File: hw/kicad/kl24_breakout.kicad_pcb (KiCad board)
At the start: 2 copper layers, 36.1 x 20.8 mm, 53 parts, among them J1 USB-micro-ab, P1 TST, P10 TST, P11 TST, P12 TST, P13 TST, P14 TST, P15 TST, P16 TST, P17 TST, P18 TST, P19 TST, P2 TST, P20 TST, P21 TST, P22 TST, P23 TST, P24 TST, P25 TST, P26 TST, P27 TST, P28 TST, P29 TST, P3 TST, P30 TST, P31 TST, P32 TST, P33 USB_V, P34 USB_GND, P35 SWD_VCC, P36 SWDIO, P37 SWCLK, P38 NRESET, P39 SWD_GND, P4 TST, P5 TST, P6 TST, P7 TST, P8 TST, P9 TST, U1 MKL24Z64VFM4, U2 LP3985, X1 CRYSTAL

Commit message: more pcb
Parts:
- C1, C2, C3, C4, D1, J1, JP1, R1, R2, R3, R4, U2: moved to B.Cu
- P33: value USB_V -> 5V
- P34: value USB_GND -> GND
- P35: value SWD_VCC -> 3.3V; footprint TEST_0.100 -> smd_simple_pad; moved to B.Cu
- P36, P37: footprint TEST_0.100 -> smd_simple_pad; moved to B.Cu
- P38: value NRESET -> NRST; footprint TEST_0.100 -> smd_simple_pad; moved to B.Cu
- P39: value SWD_GND -> GND; footprint TEST_0.100 -> smd_simple_pad; moved to B.Cu
- moved P38 39.1 mm to (141.7, 69.1), turned to 90 degrees
- moved P37 37.5 mm to (141.7, 67.1), turned to 90 degrees
- moved P36 34.8 mm to (141.7, 71.1), turned to 90 degrees
- moved P39 30.6 mm to (141.7, 73.2), turned to 90 degrees
- moved P35 30.1 mm to (141.7, 75.2), turned to 90 degrees
- moved U2 27.9 mm to (119.1, 67.8), turned to 90 degrees
- moved R3 18.1 mm to (119.6, 73.9)
- moved C4 17.7 mm to (121.4, 70.9)
- moved R4 8.40 mm to (133.6, 84.6)
- moved R1 6.28 mm to (122.9, 87.9)
- moved C2 5.80 mm to (136.1, 87.4)
- moved R2 5.61 mm to (127.5, 88.6)
- moved C3 4.60 mm to (129.3, 84.8)
- moved C1 4.34 mm to (131.8, 88.1)
- moved JP1 2.84 mm to (139.7, 85.3)
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
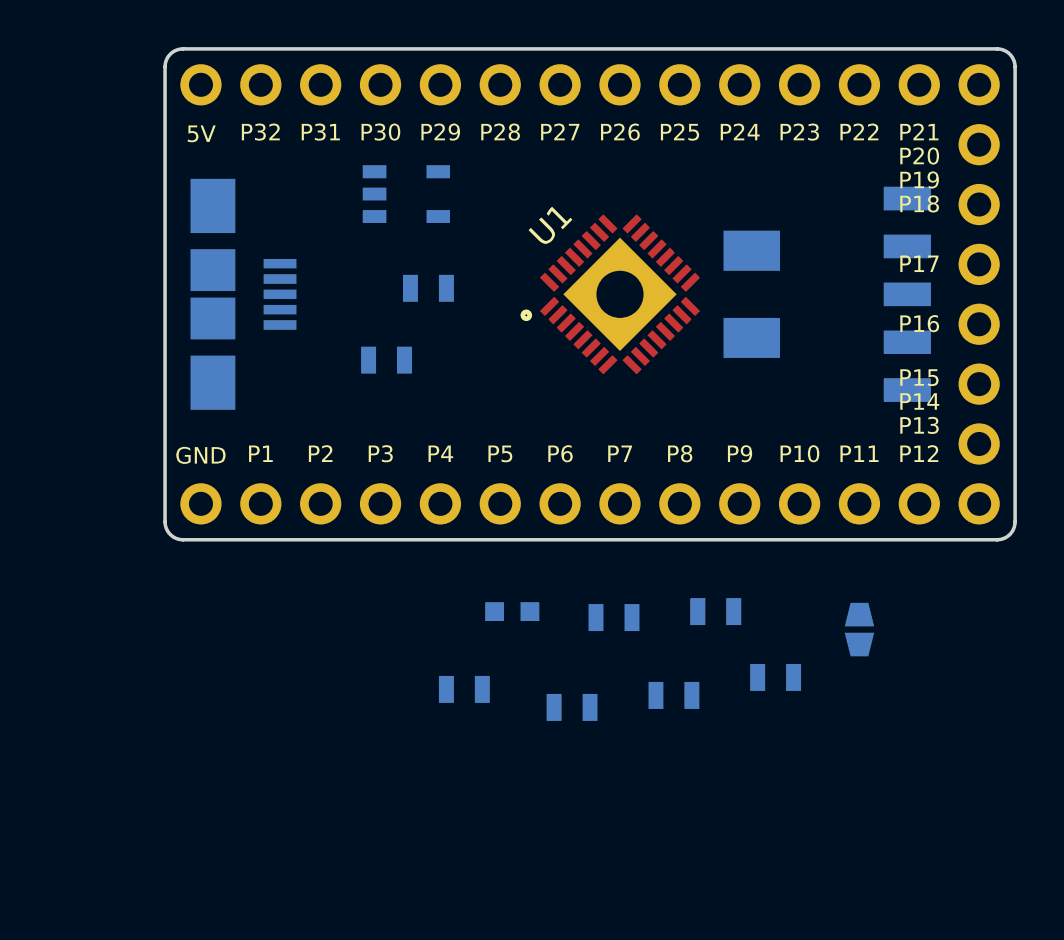
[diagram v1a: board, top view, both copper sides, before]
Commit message: all footprints placed, start wiring
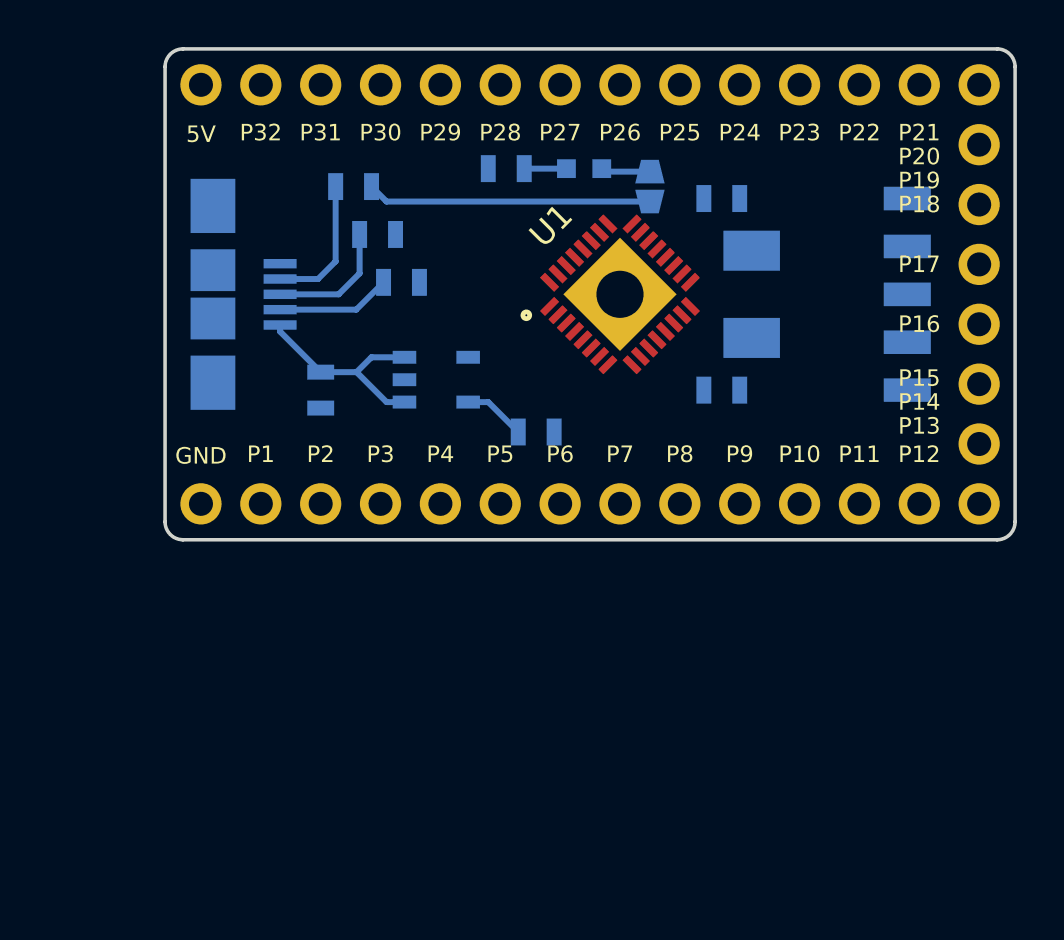
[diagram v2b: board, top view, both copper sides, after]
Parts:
- moved C1 21.2 mm to (133.9, 67.1), turned to 180 degrees
- moved R4 20.8 mm to (124.7, 65.8), turned to 180 degrees
- moved JP1 20.8 mm to (130.8, 66.5)
- moved R1 19.7 mm to (119.3, 68.6)
- moved R2 19.4 mm to (120.3, 70.6)
- moved D1 19.0 mm to (128.0, 65.8), turned to 180 degrees
- moved C3 15.8 mm to (116.8, 75.2), turned to 270 degrees
- moved C2 12.4 mm to (133.9, 75.2), turned to 180 degrees
- moved U2 7.98 mm to (120.4, 75.7)
- moved C4 7.62 mm to (126.0, 77.0)
- moved R3 7.50 mm to (118.2, 66.5)
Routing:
- net 20: track 0.00 -> 12.1 mm
- net USB_VBUS: track 0.00 -> 9.10 mm
- net Net-<J1-Pad4>: track 0.00 -> 5.84 mm
- net USB_DP: track 0.00 -> 5.39 mm
- net USB_DM: track 0.00 -> 4.87 mm
- net 7: track 0.00 -> 2.65 mm
- net Net-<D1-Pad1>: track 0.00 -> 2.10 mm
- net Net-<D1-Pad2>: track 0.00 -> 1.79 mm

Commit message: most connections
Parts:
- P33: value 5V -> USB_V
- P34: value GND -> USB_GND
- P35: value 3.3V -> SWD_VCC
- P38: value NRST -> NRESET
- P39: value GND -> SWD_GND
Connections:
- net Net-<D1-Pad1> renamed N-0000030
- net Net-<D1-Pad2> renamed N-0000031
- net Net-<J1-Pad4> renamed N-0000029
- C1 pad 2: 8 -> 16
- C2 pad 2: 8 -> 16
- C3 pad 2: 8 -> 16
- C4 pad 1: 7 -> 15
- C4 pad 2: 8 -> 16
- J1 pad 5: 8 -> 16
- J1 pad 6: 8 -> 16
- P2 pad 1: 8 -> 16
- P34 pad 1: 8 -> 16
- P35 pad 1: 7 -> 15
- P39 pad 1: 8 -> 16
- P7 pad 1: 7 -> 15
- P8 pad 1: 8 -> 16
- R4 pad 2: 8 -> 16
- U1 pad 2: 8 -> 16
- U1 pad 7: 7 -> 15
- U1 pad 8: 8 -> 16
- U2 pad 2: 8 -> 16
- U2 pad 4: Net-<U2-Pad4> -> (no net)
- U2 pad 5: 7 -> 15
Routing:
- net 16: track 0.00 -> 33.1 mm
- net 15: track 0.00 -> 23.6 mm
- net 20: track 12.1 -> 28.4 mm
- net 13: track 0.00 -> 16.3 mm
- net 18: track 0.00 -> 16.2 mm
- net 32: track 0.00 -> 15.7 mm
- net 1: track 0.00 -> 15.7 mm
- net 14: track 0.00 -> 15.1 mm
- net 19: track 0.00 -> 15.1 mm
- net 17: track 0.00 -> 15.0 mm
- net 21: track 0.00 -> 14.3 mm
- net 12: track 0.00 -> 14.0 mm
- net USB_VBUS: track 9.10 -> 22.9 mm, vias 0 -> 1
- net 31: track 0.00 -> 13.4 mm
- net 11: track 0.00 -> 11.7 mm
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- added copper zone on B.Cu, net 16
- added copper zone on F.Cu, net 16
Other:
- net class Default: clearance 0.254 -> 0.127
- rule trace_clearance: 0.254 -> 0.127

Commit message: tweak pcb
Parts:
- moved C1 8.13 mm to (133.9, 75.2)
- moved C2 8.13 mm to (133.9, 67.1)
- moved C4 0.57 mm to (125.7, 76.5), turned to 270 degrees
- turned X1 to 270 degrees
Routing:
- net 15: track 23.6 -> 47.0 mm
- net 3: track 11.1 -> 21.0 mm, vias 0 -> 1
- net 4: track 9.67 -> 19.4 mm
- net 17: track 15.0 -> 18.4 mm, vias 0 -> 1
- net 18: track 16.2 -> 18.5 mm, vias 0 -> 1
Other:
- net class Default: via_dia 0.889 -> 0.6858; via_drill 0.635 -> 0.3302
- rule via_min_drill: 0.508 -> 0.3302
- rule via_min_size: 0.889 -> 0.6858

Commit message: finish pcb, add label text
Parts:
- removed C3, C4: 1uF, SM0603
- removed U2: LP3985, LP3985
- P33: value USB_V -> +5V
- P34: value USB_GND -> GND
- moved P33 17.8 mm to (111.8, 80.0)
- moved P34 17.8 mm to (111.8, 62.2)
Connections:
- J1 pad 1: USB_VBUS -> 6
- P33 pad 1: USB_VBUS -> 6
- P5 pad 1: 5 -> 15
- U1 pad 5: 5 -> 15
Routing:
- net 6: track 7.16 -> 31.2 mm
- net USB_VBUS: track 22.9 -> 0.00 mm, vias 1 -> 0
- net 10: track 9.35 -> 24.5 mm
- net 13: track 16.3 -> 29.6 mm
- net 20: track 28.4 -> 39.4 mm, vias 0 -> 1
- net 5: track 8.42 -> 0.00 mm
- net 4: track 19.4 -> 15.9 mm, vias 0 -> 1
- net 16: track 33.1 -> 36.5 mm
- net 19: track 15.1 -> 18.4 mm, vias 0 -> 1
- net 3: track 21.0 -> 19.6 mm
- net 17: track 18.4 -> 19.5 mm
- net 18: track 18.5 -> 19.2 mm
- net 15: track 47.0 -> 46.9 mm, vias 0 -> 3
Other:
- board text added: "MKL24Z64VFM4 Breakout v0.1 git.io/7Xh66w oct-2013"
